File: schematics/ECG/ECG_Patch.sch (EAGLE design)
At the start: 6 parts

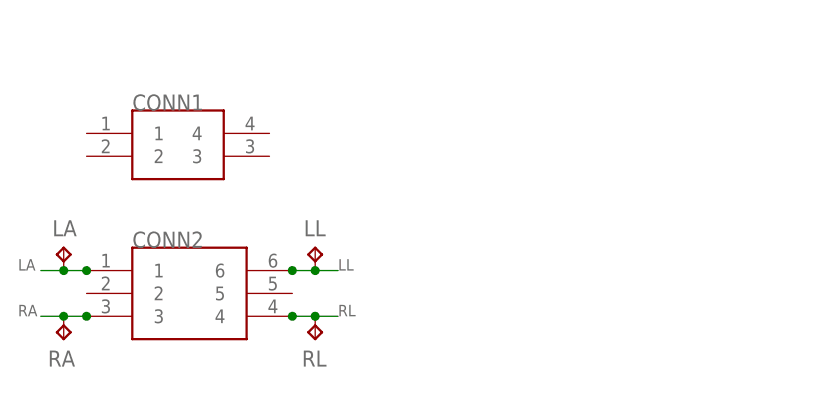
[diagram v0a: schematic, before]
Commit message: added 4 pin smt header
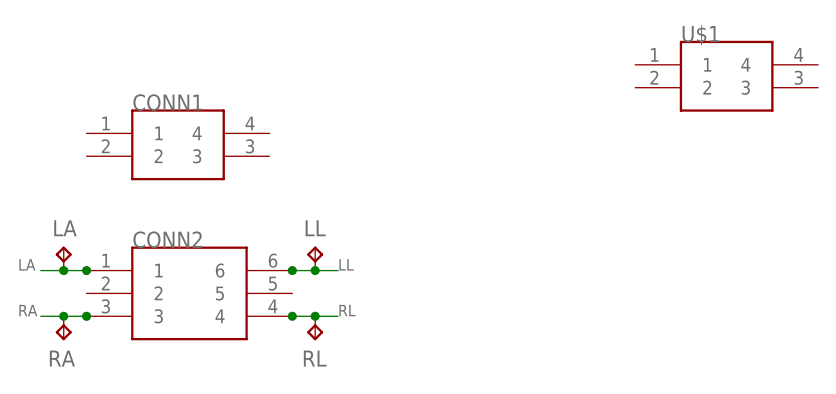
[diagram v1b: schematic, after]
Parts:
- added U$1: M80-4SMT, harwin:M80-4SMT
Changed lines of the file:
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@@
 <part name="RA" library="testpad" deviceset="TP" device="TP20R"/>
 <part name="RL" library="testpad" deviceset="TP" device="TP20R"/>
+<part name="U$1" library="harwin" deviceset="M80-4" device="SMT"/>
 </parts>
 <sheets>
@@
 <instance part="RA" gate="G$1" x="10.16" y="35.56" rot="R180"/>
 <instance part="RL" gate="G$1" x="38.1" y="35.56" rot="R180"/>
+<instance part="U$1" gate="CONN" x="83.82" y="63.5"/>
 </instances>
 <busses>
